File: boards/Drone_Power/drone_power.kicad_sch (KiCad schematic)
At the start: 8 parts, among them U1 TPS563300

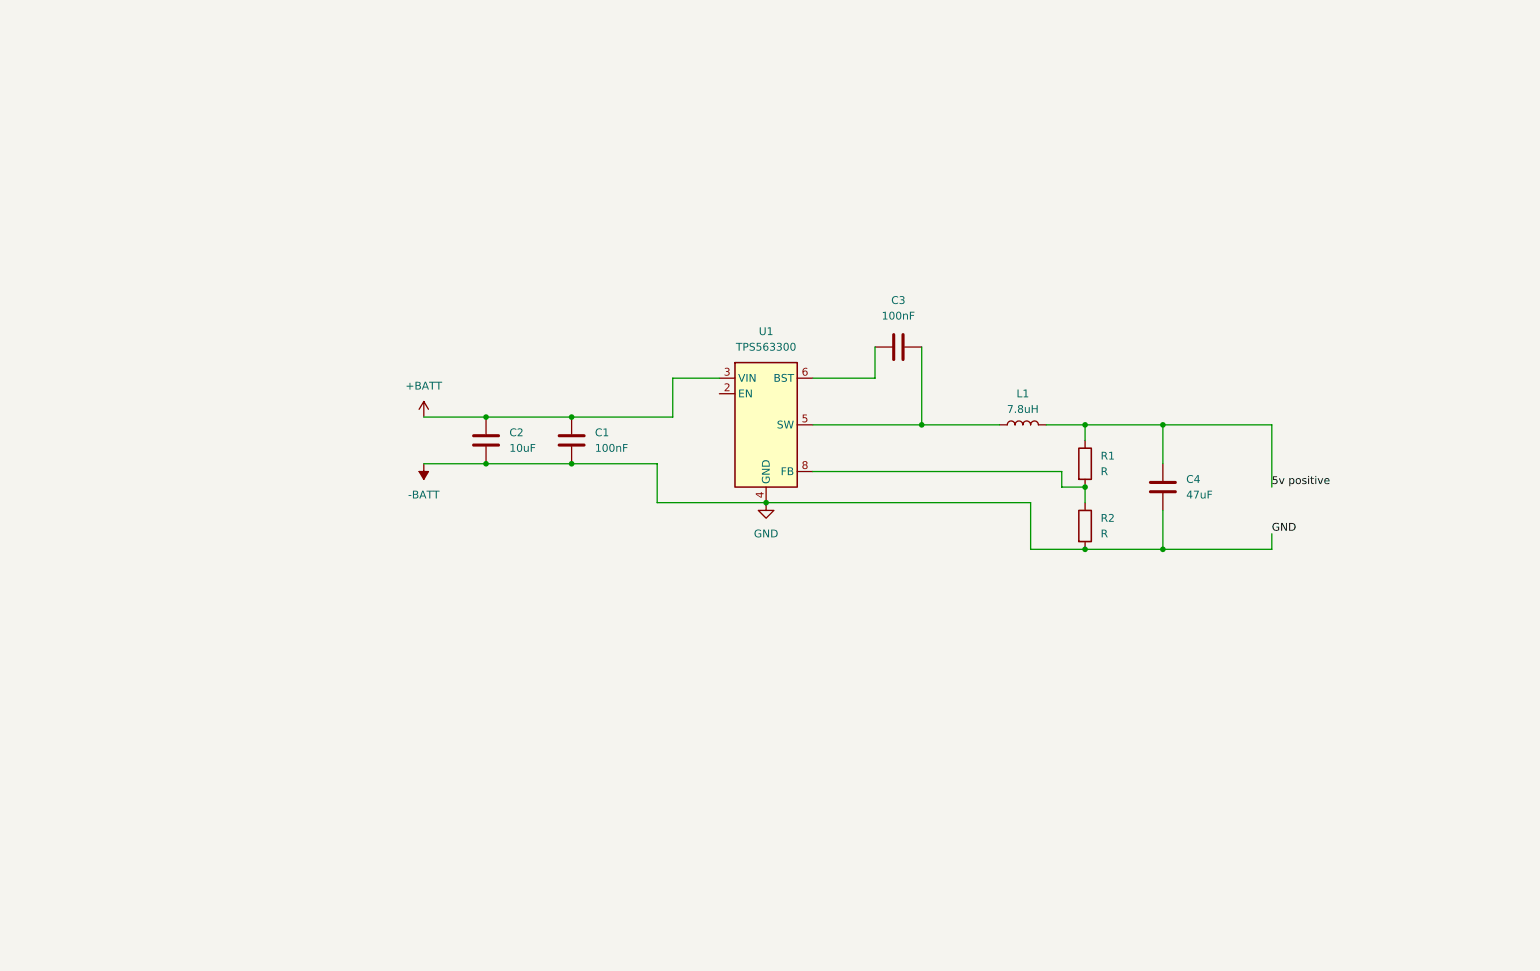
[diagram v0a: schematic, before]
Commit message: added new footprints and in PCB added new 5v and 12 groups
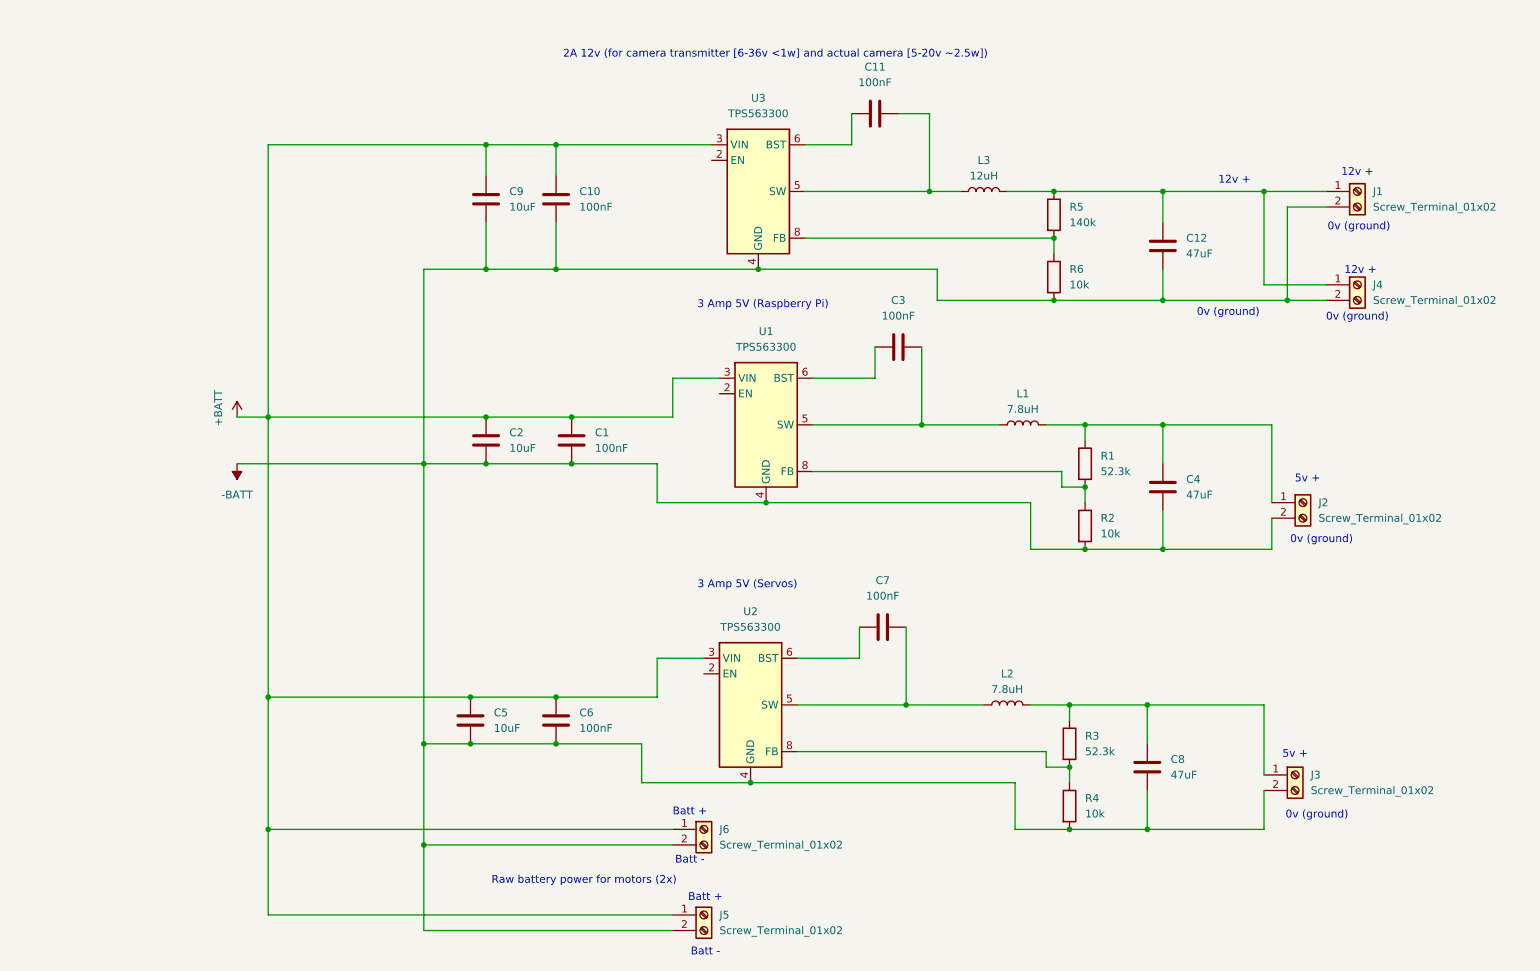
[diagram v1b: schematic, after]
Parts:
- added C10, C11, C6, C7: 100nF, symbol Device:C
- added C12, C8: 47uF, symbol Device:C
- added C5, C9: 10uF, symbol Device:C
- added J1, J2, J3, J4, J5, J6: Screw_Terminal_01x02, Connector_TE_Terminal-Block:TE_282837-2, symbol Connector:Screw_Terminal_01x02
- added L2: 7.8uH, symbol Device:L
- added L3: 12uH, Inductor_Coilcraft:IND_XGL6060_COC, symbol Device:L
- added R3: 52.3k, Resistor_SMD:R_0603_1608Metric, symbol Device:R
- added R4, R6: 10k, Resistor_SMD:R_0603_1608Metric, symbol Device:R
- added R5: 140k, Resistor_SMD:R_0603_1608Metric, symbol Device:R
- added U2, U3: TPS563300, Package_TO_SOT_SMD:SOT-583-8, symbol Regulator_Switching:TPS563300
- R1: value R -> 52.3k; footprint (none) -> Resistor_SMD:R_0603_1608Metric
- R2: value R -> 10k; footprint (none) -> Resistor_SMD:R_0603_1608Metric
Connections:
- net +BATT: now also C10.1, C5.1, C6.1, C9.1, J5.1 (Pin_1), J6.1 (Pin_1), U2.3 (VIN), U3.3 (VIN)
- net -BATT: now also C10.2, C12.2, C5.2, C6.2, C8.2, C9.2, J1.2 (Pin_2), J2.2 (Pin_2), J3.2 (Pin_2), J4.2 (Pin_2), J5.2 (Pin_2), J6.2 (Pin_2), R4.2, R6.2, U2.4 (GND), U3.4 (GND)
- net 5v positive: no longer names the net of C4.1, L1.2, R1.1
- net 5v positive: now also J2.1 (Pin_1)
- new net: R5.2, R6.1, U3.8 (FB)
- new net: C11.1, U3.6 (BST)
- new net: C11.2, L3.1, U3.5 (SW)
- new net: R3.2, R4.1, U2.8 (FB)
- new net: C8.1, J3.1 (Pin_1), L2.2, R3.1
- new net: C12.1, J1.1 (Pin_1), J4.1 (Pin_1), L3.2, R5.1
- new net: C7.2, L2.1, U2.5 (SW)
- new net: C7.1, U2.6 (BST)
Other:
- note added: "0v (ground)"
- note added: "12v +"
- note added: "2A 12v (for camera transmitter [6-36v <1w] and actual camera [5-20v ~2.5w])"
- note added: "3 Amp 5V (Raspberry Pi)"
- note added: "3 Amp 5V (Servos)"
- note added: "5v +"
- note added: "Batt +"
- note added: "Batt -"
- note added: "Raw battery power for motors (2x)"

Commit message: actually doing it
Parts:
- C1, C10, C11, C3, C6, C7: footprint (none) -> Capacitor_SMD:C_0603_1608Metric
- C12, C4, C8: footprint (none) -> Capacitor_SMD:C_1210_3225Metric
- C2, C5, C9: footprint (none) -> Capacitor_SMD:C_1206_3216Metric
- L1, L2: footprint (none) -> Inductor_SMD:L_Wuerth_HCI-1050
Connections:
- no-connect marks 0 -> 3
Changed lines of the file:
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@@
 		(color 0 0 0 0)
 	)
+	(no_connect
+		(at 127 133.35)
+	)
+	(no_connect
+		(at 128.27 49.53)
+	)
+	(no_connect
+		(at 129.54 87.63)
+	)
 	(wire
 		(pts
@@
 			)
 		)
-		(property "Footprint" ""
+		(property "Footprint" "Capacitor_SMD:C_0603_1608Metric"
 			(at 103.8352 144.78 0)
 			(effects
@@
 			)
 		)
-		(property "Footprint" ""
+		(property "Footprint" "Capacitor_SMD:C_1210_3225Metric"
 			(at 202.8952 106.68 0)
 			(effects
@@
 			)
 		)
-		(property "Footprint" ""
+		(property "Footprint" "Capacitor_SMD:C_1206_3216Metric"
 			(at 92.4052 59.69 0)
 			(effects
@@
 			)
 		)
-		(property "Footprint" ""
+		(property "Footprint" "Capacitor_SMD:C_0603_1608Metric"
 			(at 158.75 40.9448 0)
 			(effects
@@
 			)
 		)
-		(property "Footprint" ""
+		(property "Footprint" "Capacitor_SMD:C_1210_3225Metric"
 			(at 200.3552 152.4 0)
 			(effects
@@
 			)
 		)
-		(property "Footprint" ""
+		(property "Footprint" "Capacitor_SMD:C_0603_1608Metric"
 			(at 103.8352 59.69 0)
 			(effects
@@
 			)
 		)
-		(property "Footprint" ""
+		(property "Footprint" "Inductor_SMD:L_Wuerth_HCI-1050"
 			(at 179.07 92.71 0)
 			(effects
@@
 			)
 		)
-		(property "Datasheet" "~"
+		(property "Datasheet" "https://www.we-online.com/components/products/datasheet/744325780.pdf"
 			(at 179.07 92.71 0)
 			(effects
@@
 			)
 		)
-		(property "Footprint" ""
+		(property "Footprint" "Inductor_SMD:L_Wuerth_HCI-1050"
 			(at 176.53 138.43 0)
 			(effects
@@
 			)
 		)
-		(property "Datasheet" "~"
+		(property "Datasheet" "https://www.we-online.com/components/products/datasheet/744325780.pdf"
 			(at 176.53 138.43 0)
 			(effects
@@
 			)
 		)
-		(property "Footprint" ""
+		(property "Footprint" "Capacitor_SMD:C_0603_1608Metric"
 			(at 162.56 79.0448 0)
 			(effects
@@
 			)
 		)
-		(property "Footprint" ""
+		(property "Footprint" "Capacitor_SMD:C_0603_1608Metric"
 			(at 106.3752 99.06 0)
 			(effects
@@
 			)
 		)
-		(property "Footprint" ""
+		(property "Footprint" "Capacitor_SMD:C_0603_1608Metric"
 			(at 160.02 124.7648 0)
 			(effects
@@
 			)
 		)
-		(property "Footprint" ""
+		(property "Footprint" "Capacitor_SMD:C_1206_3216Metric"
 			(at 89.8652 144.78 0)
 			(effects
@@
 			)
 		)
-		(property "Footprint" ""
+		(property "Footprint" "Capacitor_SMD:C_1206_3216Metric"
 			(at 92.4052 99.06 0)
 			(effects
@@
 			)
 		)
-		(property "Footprint" ""
+		(property "Footprint" "Capacitor_SMD:C_1210_3225Metric"
 			(at 202.8952 67.31 0)
 			(effects

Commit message: even smallergit status!
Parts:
- removed J5, J6: Screw_Terminal_01x02, Connector_TE_Terminal-Block:TE_282837-2, symbol Connector:Screw_Terminal_01x02
- added H1, H2: MountingHole_Pad, MountingHole:MountingHole_3mm_Pad_Via, symbol Mechanical:MountingHole_Pad
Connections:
- no-connect marks 3 -> 5
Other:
- note removed: "Batt +"
- note removed: "Batt -"
- note removed: "Raw battery power for motors (2x)"

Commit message: dawwwwg
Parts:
- added H3: MountingHole_Pad, MountingHole:MountingHole_3mm_Pad_Via, symbol Mechanical:MountingHole_Pad
- added J5: Screw_Terminal_01x02, Connector_TE_Terminal-Block:TE_282837-2, symbol Connector:Screw_Terminal_01x02
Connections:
- net +BATT: no longer names the net of C1.1, C10.1, C2.1, C5.1, C6.1, C9.1, U1.3 (VIN), U2.3 (VIN), U3.3 (VIN)
- net +BATT: now also J5.1 (Pin_1)
- net -BATT: no longer names the net of C1.2, C10.2, C12.2, C2.2, C4.2, C5.2, C6.2, C8.2, C9.2, J1.2 (Pin_2), J2.2 (Pin_2), J3.2 (Pin_2), J4.2 (Pin_2), R2.2, R4.2, R6.2, U1.4 (GND), U2.4 (GND), U3.4 (GND)
- net -BATT: now also J5.2 (Pin_2)
- no-connect marks 5 -> 6
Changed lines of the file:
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@@
 	)
 	(no_connect
+		(at 50.8 48.26)
+	)
+	(no_connect
 		(at 50.8 31.75)
 	)
@@
 	(wire
 		(pts
+			(xy 46.99 96.52) (xy 50.8 96.52)
+		)
+		(stroke
+			(width 0)
+			(type default)
+		)
+	)
+	(wire
+		(pts
 			(xy 91.44 91.44) (xy 105.41 91.44)
 		)
@@
 	(wire
 		(pts
+			(xy 50.8 93.98) (xy 50.8 91.44)
+		)
+		(stroke
+			(width 0)
+			(type default)
+		)
+	)
+	(wire
+		(pts
 			(xy 189.23 92.71) (xy 201.93 92.71)
 		)
@@
 	(wire
 		(pts
+			(xy 46.99 93.98) (xy 50.8 93.98)
+		)
+		(stroke
+			(width 0)
+			(type default)
+		)
+	)
+	(wire
+		(pts
 			(xy 180.34 113.03) (xy 189.23 113.03)
 		)
@@
 	(wire
 		(pts
+			(xy 50.8 96.52) (xy 50.8 99.06)
+		)
+		(stroke
+			(width 0)
+			(type default)
+		)
+	)
+	(wire
+		(pts
 			(xy 184.15 72.39) (xy 165.1 72.39)
 		)
@@
 		)
 	)
+	(text "0v (ground)"
+		(exclude_from_sim no)
+		(at 41.656 90.678 0)
+		(effects
+			(font
+				(size 1.27 1.27)
+			)
+		)
+	)
 	(text "3 Amp 5V (Raspberry Pi)"
 		(exclude_from_sim no)
@@
 	(text "12v +\n"
 		(exclude_from_sim no)
+		(at 41.91 99.568 0)
+		(effects
+			(font
+				(size 1.27 1.27)
+			)
+		)
+	)
+	(text "12v +\n"
+		(exclude_from_sim no)
 		(at 234.188 67.564 0)
 		(effects
@@
 	)
 	(symbol
+		(lib_id "Mechanical:MountingHole_Pad")
+		(at 50.8 45.72 0)
+		(unit 1)
+		(exclude_from_sim yes)
+		(in_bom no)
+		(on_board yes)
+		(dnp no)
+		(fields_autoplaced yes)
+		(property "Reference" "H3"
+			(at 53.34 43.1799 0)
+			(effects
+				(font
+					(size 1.27 1.27)
+				)
+				(justify left)
+			)
+		)
+		(property "Value" "MountingHole_Pad"
+			(at 53.34 45.7199 0)
+			(effects
+				(font
+					(size 1.27 1.27)
+				)
+				(justify left)
+			)
+		)
+		(property "Footprint" "MountingHole:MountingHole_3mm_Pad_Via"
+			(at 50.8 45.72 0)
+			(effects
+				(font
+					(size 1.27 1.27)
+				)
+				(hide yes)
+			)
+		)
+		(property "Datasheet" "~"
+			(at 50.8 45.72 0)
+			(effects
+				(font
+					(size 1.27 1.27)
+				)
+				(hide yes)
+			)
+		)
+		(property "Description" "Mounting Hole with connection"
+			(at 50.8 45.72 0)
+			(effects
+				(font
+					(size 1.27 1.27)
+				)
+				(hide yes)
+			)
+		)
+		(pin "1"
+		)
+		(instances
+			(project "drone_power"
+				(path "/d57d17ab-494b-4c11-a4da-cdc1a6c16e8e"
+					(reference "H3")
+					(unit 1)
+				)
+			)
+		)
+	)
+	(symbol
 		(lib_id "Device:R")
 		(at 189.23 99.06 0)
@@
 	(symbol
 		(lib_id "Connector:Screw_Terminal_01x02")
+		(at 41.91 93.98 0)
+		(mirror y)
+		(unit 1)
+		(exclude_from_sim no)
+		(in_bom yes)
+		(on_board yes)
+		(dnp no)
+		(property "Reference" "J5"
+			(at 39.37 93.9799 0)
+			(effects
+				(font
+					(size 1.27 1.27)
+				)
+				(justify left)
+			)
+		)
+		(property "Value" "Screw_Terminal_01x02"
+			(at 39.37 96.5199 0)
+			(effects
+				(font
+					(size 1.27 1.27)
+				)
+				(justify left)
+			)
+		)
+		(property "Footprint" "Connector_TE_Terminal-Block:TE_282837-2"
+			(at 41.91 93.98 0)
+			(effects
+				(font
+					(size 1.27 1.27)
+				)
+				(hide yes)
+			)
+		)
+		(property "Datasheet" "~"
+			(at 41.91 93.98 0)
+			(effects
+				(font
+					(size 1.27 1.27)
+				)
+				(hide yes)
+			)
+		)
+		(property "Description" "Generic screw terminal, single row, 01x02, script generated (kicad-library-utils/schlib/autogen/connector/)"
+			(at 41.91 93.98 0)
+			(effects
+				(font
+					(size 1.27 1.27)
+				)
+				(hide yes)
+			)
+		)
+		(pin "1"
+		)
+		(pin "2"
+		)
+		(instances
+			(project "drone_power"
+				(path "/d57d17ab-494b-4c11-a4da-cdc1a6c16e8e"
+					(reference "J5")
+					(unit 1)
+				)
+			)
+		)
+	)
+	(symbol
+		(lib_id "Connector:Screw_Terminal_01x02")
 		(at 233.68 54.61 0)
 		(unit 1)
@@
 	)
 	(symbol
-		(lib_id "power:-BATT")
-		(at 50.8 99.06 180)
-		(unit 1)
-		(exclude_from_sim no)
-		(in_bom yes)
-		(on_board yes)
-		(dnp no)
-		(fields_autoplaced yes)
-		(property "Reference" "#PWR02"
-			(at 50.8 95.25 0)
-			(effects
-				(font
-					(size 1.27 1.27)
-				)
-				(hide yes)
-			)
-		)
-		(property "Value" "-BATT"
-			(at 50.8 104.14 0)
-			(effects
-				(font
-					(size 1.27 1.27)
-				)
-			)
-		)
-		(property "Footprint" ""
-			(at 50.8 99.06 0)
-			(effects
-				(font
-					(size 1.27 1.27)
-				)
-				(hide yes)
-			)
-		)
-		(property "Datasheet" ""
-			(at 50.8 99.06 0)
-			(effects
-				(font
-					(size 1.27 1.27)
-				)
-				(hide yes)
-			)
-		)
-		(property "Description" "Power symbol creates a global label with name \"-BATT\""
-			(at 50.8 99.06 0)
-			(effects
-				(font
-					(size 1.27 1.27)
-				)
-				(hide yes)
-			)
-		)
-		(pin "1"
-		)
-		(instances
-			(project ""
-				(path "/d57d17ab-494b-4c11-a4da-cdc1a6c16e8e"
-					(reference "#PWR02")
-					(unit 1)
-				)
-			)
-		)
-	)
-	(symbol
 		(lib_id "Device:C")
 		(at 91.44 95.25 0)
@@
 					(unit 1)
 				)
-			)
-		)
-	)
-	(symbol
-		(lib_id "power:+BATT")
-		(at 50.8 91.44 0)
-		(unit 1)
-		(exclude_from_sim no)
-		(in_bom yes)
-		(on_board yes)
-		(dnp no)
-		(property "Reference" "#PWR01"
-			(at 50.8 95.25 0)
-			(effects
-				(font
-					(size 1.27 1.27)
-				)
-				(hide yes)
-			)
-		)
-		(property "Value" "+BATT"
-			(at 47.752 92.964 90)
-			(effects
-				(font
-					(size 1.27 1.27)
-				)
-				(justify left)
-			)
-		)
-		(property "Footprint" ""
-			(at 50.8 91.44 0)
-			(effects
-				(font
-					(size 1.27 1.27)
-				)
-				(hide yes)
-			)
-		)
-		(property "Datasheet" ""
-			(at 50.8 91.44 0)
-			(effects
-				(font
-					(size 1.27 1.27)
-				)
-				(hide yes)
-			)
-		)
-		(property "Description" "Power symbol creates a global label with name \"+BATT\""
-			(at 50.8 91.44 0)
-			(effects
-				(font
-					(size 1.27 1.27)
-				)
-				(hide yes)
-			)
-		)
-		(pin "1"
-		)
-		(instances
-			(project ""
-				(path "/d57d17ab-494b-4c11-a4da-cdc1a6c16e8e"
-					(reference "#PWR01")
-					(unit 1)
-				)

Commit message: added some text
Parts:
- added D1: BLUE LED, LED_SMD:LED_0603_1608Metric, symbol Device:LED
- added D2: GREEN LED, LED_SMD:LED_0603_1608Metric, symbol Device:LED
- added D3: RED LED, LED_SMD:LED_0603_1608Metric, symbol Device:LED
- added R7, R8: 140, Resistor_SMD:R_0603_1608Metric, symbol Device:R_US
- added R9: 500, Resistor_SMD:R_0603_1608Metric, symbol Device:R_US
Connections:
- net at C1.2, C10.2, C12.2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: now also D1.1 (K), D2.1 (K), D3.1 (K)
- net at C4.1, J2.1 (Pin_1), L1.2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: now also R8.1
- net at C8.1, J3.1 (Pin_1), L2.2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: now also R7.1
- net at C12.1, J1.1 (Pin_1), J4.1 (Pin_1)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: now also R9.1
- new net: D1.2 (A), R7.2
- new net: D3.2 (A), R9.2
- new net: D2.2 (A), R8.2
